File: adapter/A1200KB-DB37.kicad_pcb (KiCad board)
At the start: 2 copper layers, 75 x 31.7 mm, 41 parts, among them J1 Molex 52044-3245, J2 LED HDR, J3 DB37 female RA

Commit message: add floppy power header for ground, move h1 to make room.
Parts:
- added J4: Floppy PWR (TE 171826-4), Connector_Floppy:TE_171826-4_1x04_P2.50mm_Horizontal, F.Cu at (106.2, 104.8)
- moved H1 7.52 mm to (104.0, 112.0)
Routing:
- net GND: track 42.5 -> 52.2 mm
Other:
- board text added: "J4 FDD PWR"

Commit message: replace floppy header with symmetric 5-pin led header for safe reversal.
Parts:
- removed J4: Floppy PWR (TE 171826-4), Connector_Floppy:TE_171826-4_1x04_P2.50mm_Horizontal
- J2: value LED HDR -> LED HDR (symmetric); footprint Connector_PinHeader_2.54mm:PinHeader_1x04_P2.54mm_Vertical -> Connector_PinHeader_2.54mm:PinHeader_1x05_P2.54mm_Horizontal
- moved J2 8.23 mm to (107.0, 104.5)
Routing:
- net /DISK_LED: track 15.4 -> 24.3 mm
- net /FLOPPY_LED: track 15.4 -> 24.2 mm
- net /PWRLED: track 15.5 -> 24.1 mm
- net GND: track 52.2 -> 56.7 mm
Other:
- board text added: "LED: GND PWR FLP DSK GND"
- board text removed: "J4 FDD PWR"
- board text removed: "LED: GND PWR FLP DSK"

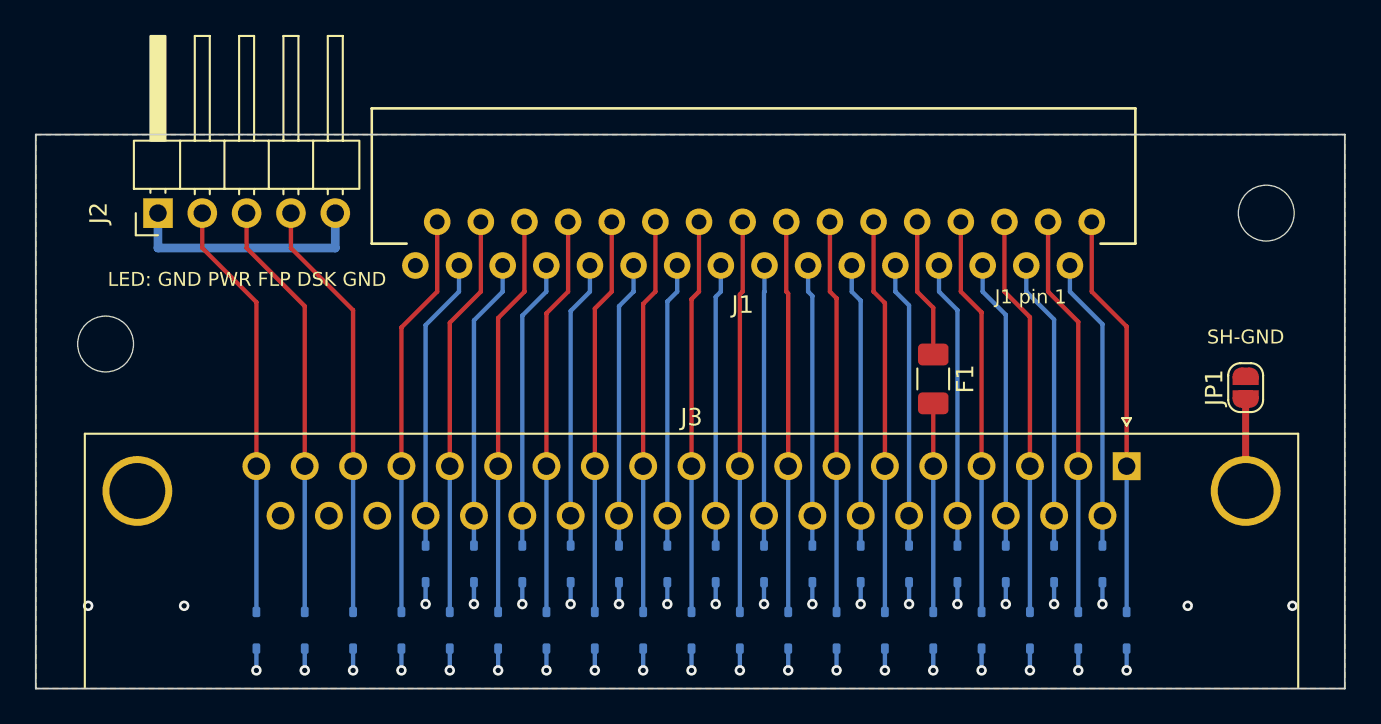
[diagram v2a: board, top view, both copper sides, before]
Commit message: refit db37 edge offset to suit the sockets lcsc actually stocks.
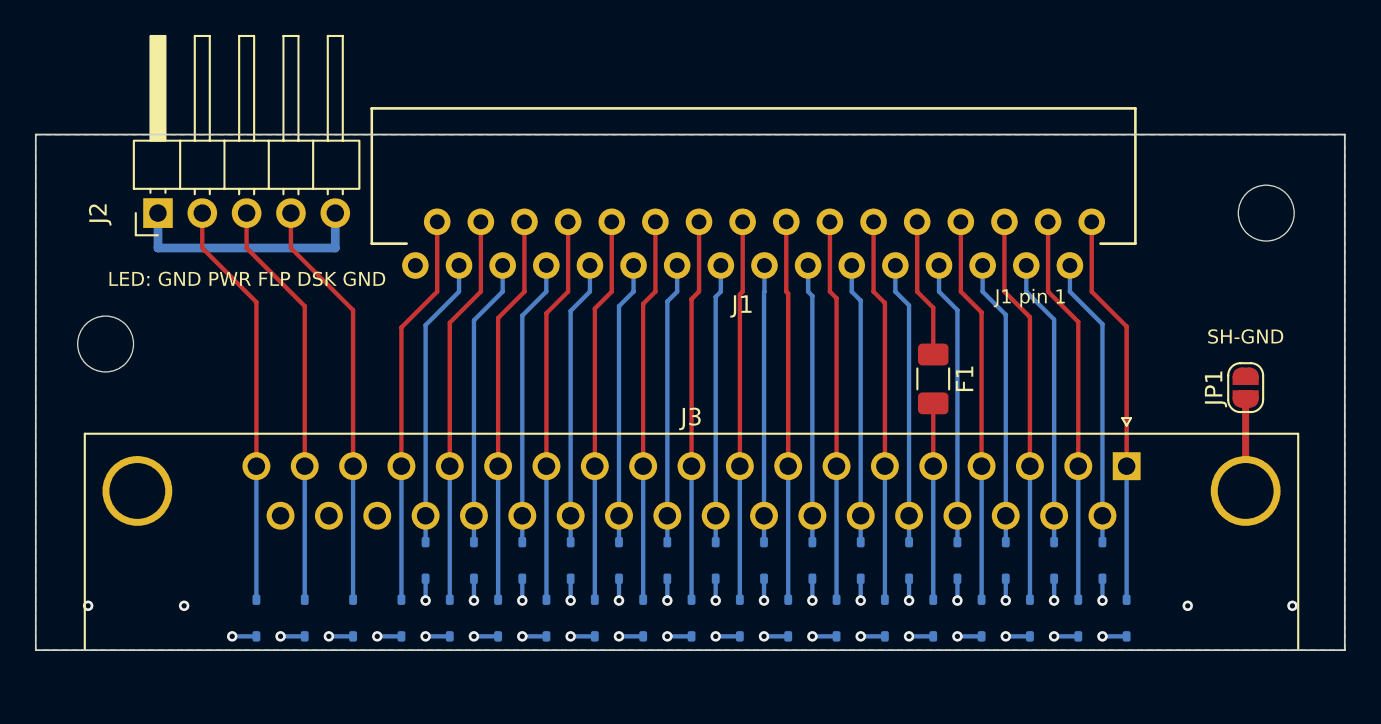
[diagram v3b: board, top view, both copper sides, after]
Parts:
- J3: footprint Connector_Dsub:DSUB-37_Socket_Horizontal_P2.77x2.84mm_EdgePinOffset9.90mm_Housed_MountingHolesOffset11.32mm -> Connector_Dsub:DSUB-37_Socket_Horizontal_P2.77x2.84mm_EdgePinOffset7.70mm_Housed_MountingHolesOffset9.12mm
- moved D1 0.70 mm to (162.5, 127.7)
- moved D10 0.70 mm to (137.6, 127.7)
- moved D11 0.70 mm to (134.8, 127.7)
- moved D12 0.70 mm to (132.0, 127.7)
- moved D13 0.70 mm to (129.3, 127.7)
- moved D14 0.70 mm to (126.5, 127.7)
- moved D15 0.70 mm to (123.7, 127.7)
- moved D16 0.70 mm to (121.0, 127.7)
- moved D17 0.70 mm to (118.2, 127.7)
- moved D18 0.70 mm to (115.4, 127.7)
- moved D19 0.70 mm to (112.6, 127.7)
- moved D2 0.70 mm to (159.7, 127.7)
- moved D3 0.70 mm to (157.0, 127.7)
- moved D4 0.70 mm to (154.2, 127.7)
- moved D5 0.70 mm to (151.4, 127.7)
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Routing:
- net GND: track 56.7 -> 59.2 mm
- net /~{CAPSLOCK}: track 23.2 -> 22.5 mm
- net /VCC_DB: track 11.9 -> 11.2 mm
- net /PWRLED: track 24.1 -> 23.4 mm
- net /KB29: track 23.1 -> 22.4 mm
- net /KB27: track 23.0 -> 22.3 mm
- net /KB25: track 22.9 -> 22.2 mm
- net /KB23: track 22.8 -> 22.1 mm
- net /KB21: track 22.6 -> 21.9 mm
- net /KB19: track 22.5 -> 21.8 mm
- net /KB17: track 22.4 -> 21.7 mm
- net /KB15: track 22.4 -> 21.7 mm
- net /KB13: track 22.5 -> 21.8 mm
- net /KB11: track 22.6 -> 21.9 mm
- net /KB07: track 22.8 -> 22.1 mm
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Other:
- board size 75 x 31.7 mm -> 75 x 29.5 mm
